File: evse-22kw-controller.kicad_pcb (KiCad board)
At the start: 4 copper layers, 100 x 80 mm, 0 parts

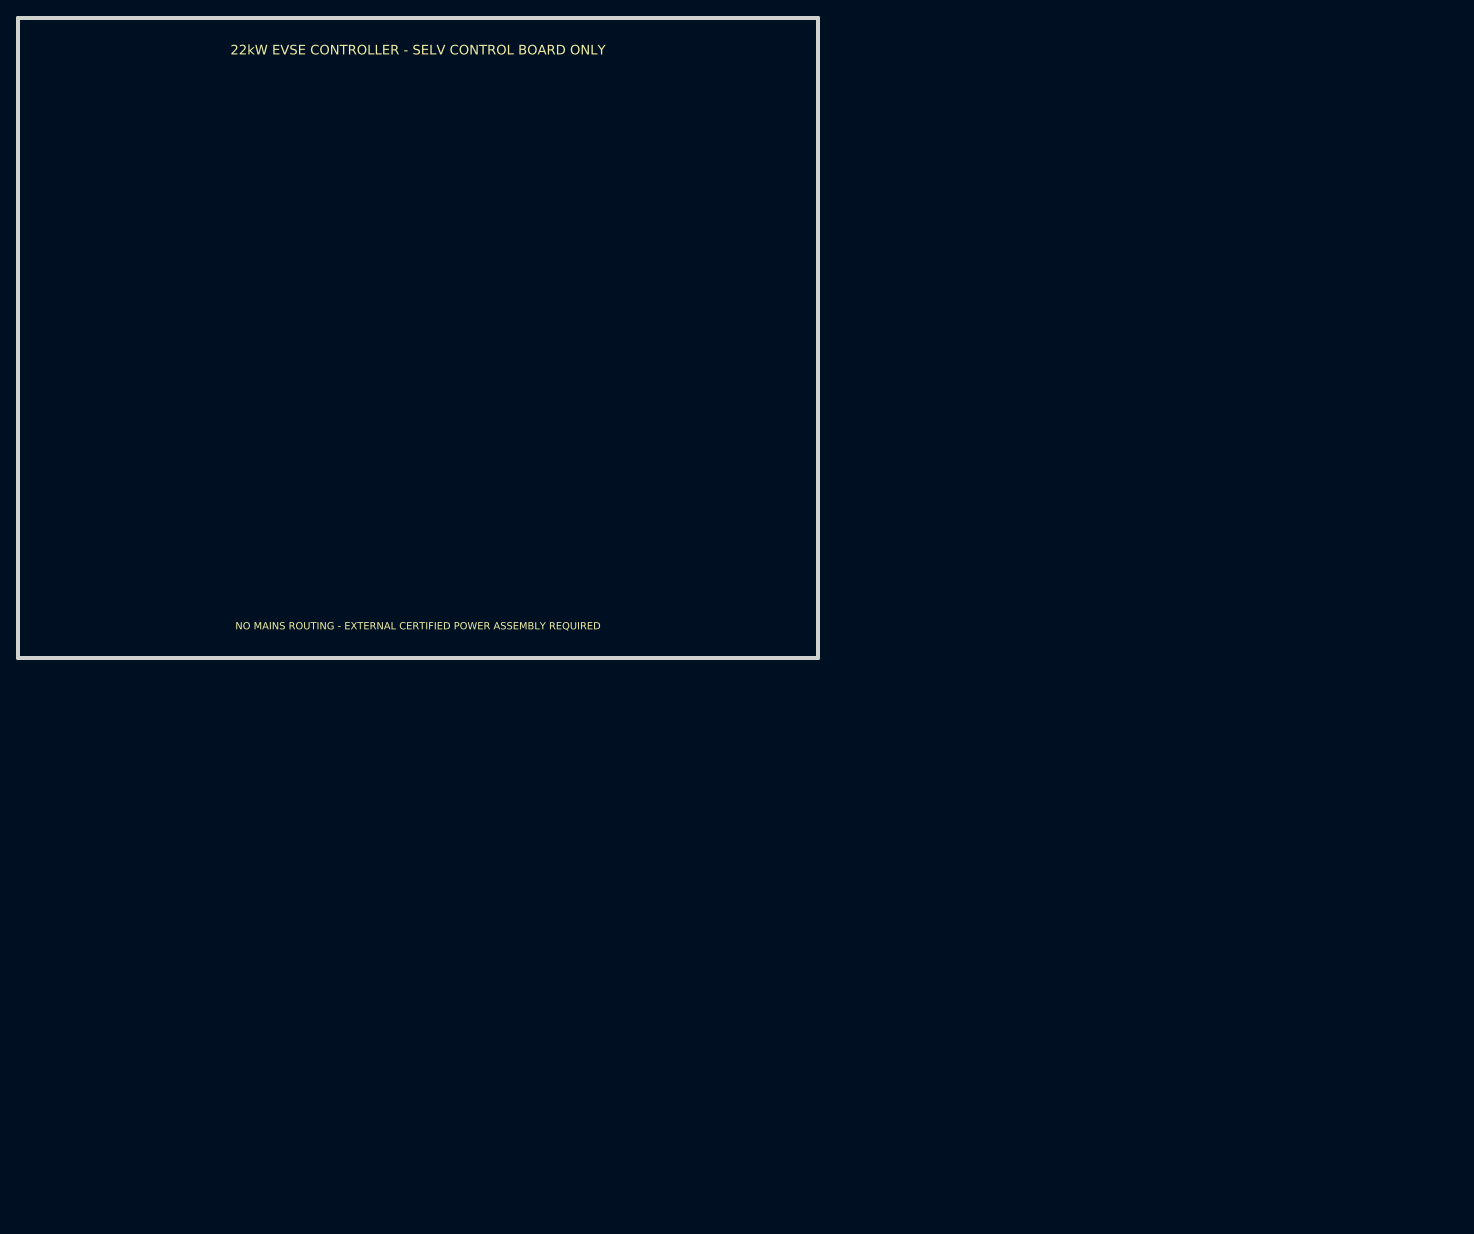
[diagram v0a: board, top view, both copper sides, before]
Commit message: Create a prototype KiCad schematic and PCB baseline for the EVSE controller control board.
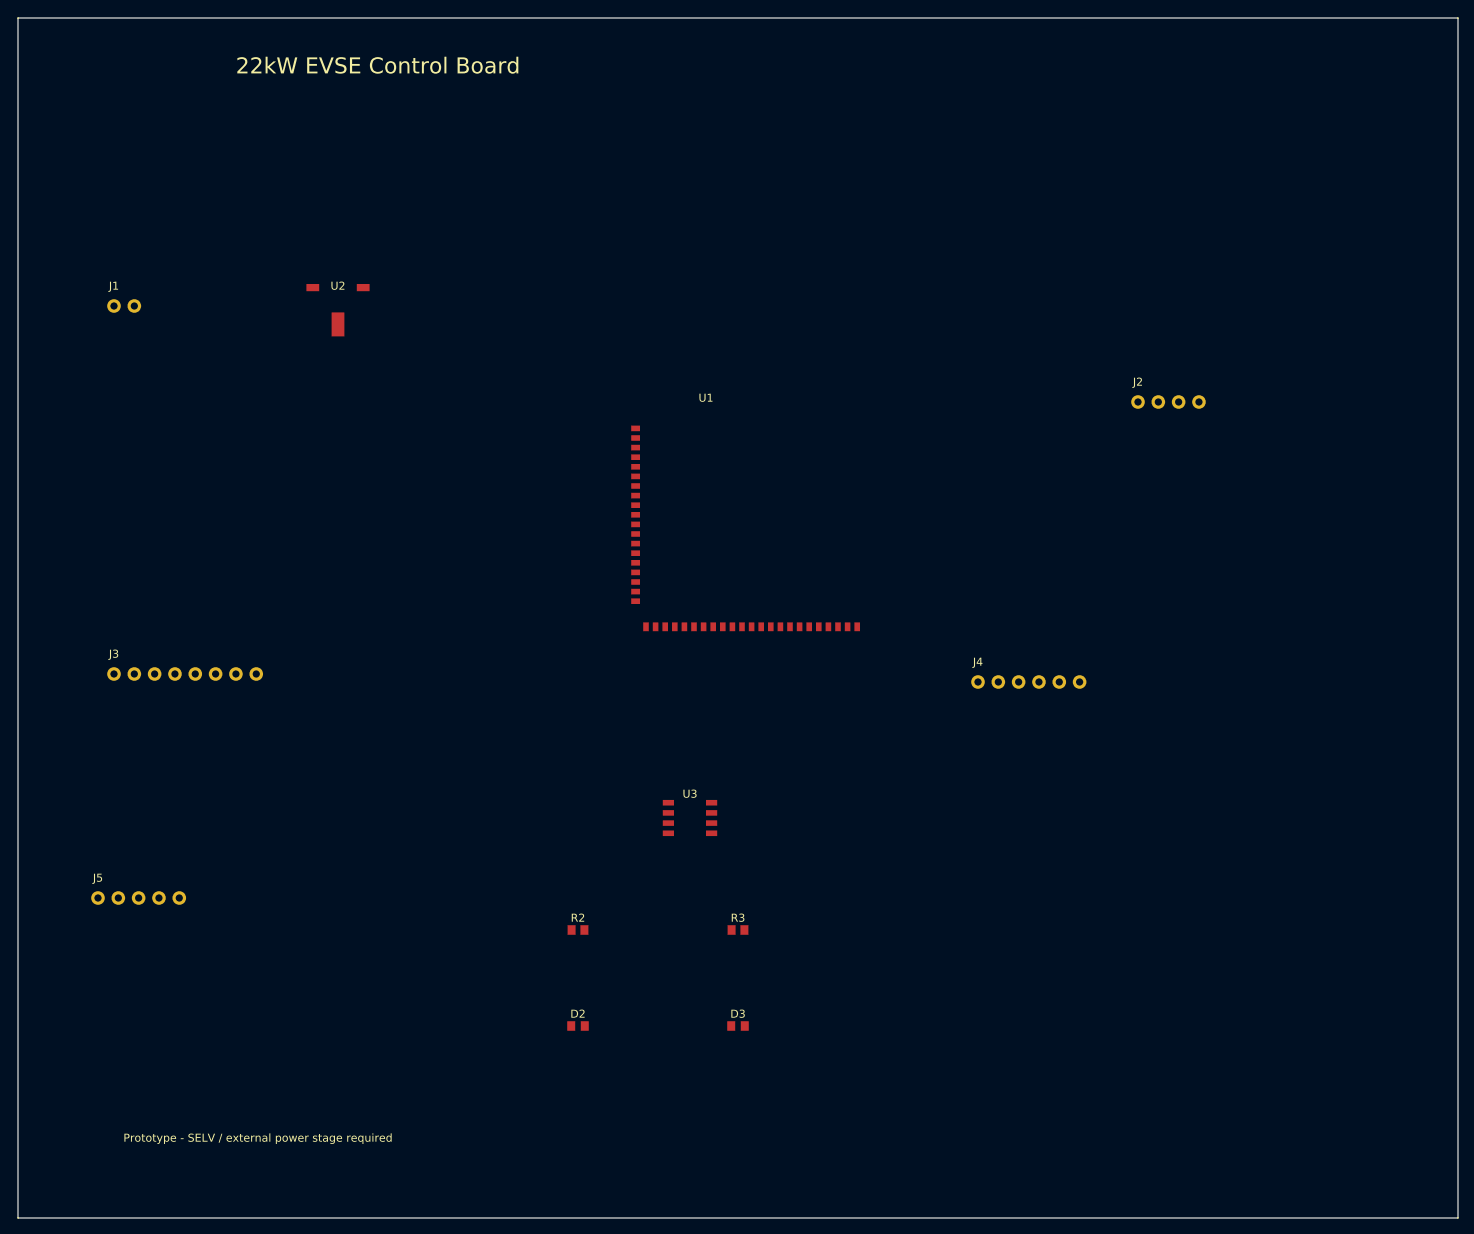
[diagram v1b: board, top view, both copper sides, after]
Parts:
- added D2: , LED_SMD:LED_0603_1608Metric, F.Cu at (90.0, 146.0)
- added D3: , LED_SMD:LED_0603_1608Metric, F.Cu at (110.0, 146.0)
- added J1: , Connector_Molex:Molex_KK-254_AE-6410-02A_1x02_P2.54mm_Vertical, F.Cu at (32.0, 56.0)
- added J2: , Connector_Molex:Molex_KK-254_AE-6410-04A_1x04_P2.54mm_Vertical, F.Cu at (160.0, 68.0)
- added J3: , Connector_Molex:Molex_KK-254_AE-6410-08A_1x08_P2.54mm_Vertical, F.Cu at (32.0, 102.0)
- added J4: , Connector_Molex:Molex_KK-254_AE-6410-06A_1x06_P2.54mm_Vertical, F.Cu at (140.0, 103.0)
- added J5: , Connector_Molex:Molex_KK-254_AE-6410-05A_1x05_P2.54mm_Vertical, F.Cu at (30.0, 130.0)
- added R2: , Resistor_SMD:R_0603_1608Metric, F.Cu at (90.0, 134.0)
- added R3: , Resistor_SMD:R_0603_1608Metric, F.Cu at (110.0, 134.0)
- added U1: , RF_Module:ESP32-S3-WROOM-1, F.Cu at (106.0, 80.0)
- added U2: , Package_TO_SOT_SMD:SOT-223-3_TabPin2, F.Cu at (60.0, 56.0)
- added U3: , Package_SO:SOIC-8_3.9x4.9mm_P1.27mm, F.Cu at (104.0, 120.0)
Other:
- board size 100 x 80 mm -> 180 x 150 mm
- copper layers 4 -> 2
- board text added: "22kW EVSE Control Board"
- board text added: "Prototype - SELV / external power stage required"
- board text removed: "22kW EVSE CONTROLLER - SELV CONTROL BOARD ONLY"
- board text removed: "NO MAINS ROUTING - EXTERNAL CERTIFIED POWER ASSEMBLY REQUIRED"
